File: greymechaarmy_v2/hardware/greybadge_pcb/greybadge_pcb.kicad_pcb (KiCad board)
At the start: 2 copper layers, 75 x 99 mm, 155 parts, among them J1 Conn_02x05_Row_Letter_First, J2 Conn_02x05_Row_Letter_First, J3 Conn_02x05_Row_Letter_First, J4 JST PH S2B, J5 USB_C_Receptacle_USB2.0, J6 Conn_02x05_Row_Letter_First, Q1 2N7002, Q2 Q_NMOS_GSD, SW1 SW_Push, SW10 SW_Push, SW2 SW_Push, SW3 SW_Push, SW4 SW_Push, SW5 SW_Push, SW6 SW_Push, SW7 SW_Push, SW8 SW_SPDT, SW9 SW_Push, U1 APS6404L-3SQR-SN_C5333729, U10 AMS1117-3.3, U2 TLV73311PDBV, U3 TLV73325PDBV, U4 GC9A01_IPS_display, U5 BQ24075, U6 W25Q128JVS, U7 RP2350_60QFN, U8 ECP5U_25_CABGA256, U9 W25Q128JVSIM, X1 SiT2001B, Y1 12Mhz

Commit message: feat: improve art
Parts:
- added G***: LOGO, LOGO, F.Cu at (96.2, 65.4)
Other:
- board text added: "C4[2] C6[6] D3[1] C5[4] D5[5] C3[0] D4[3] D6[7]"
- board text added: "LEDs"

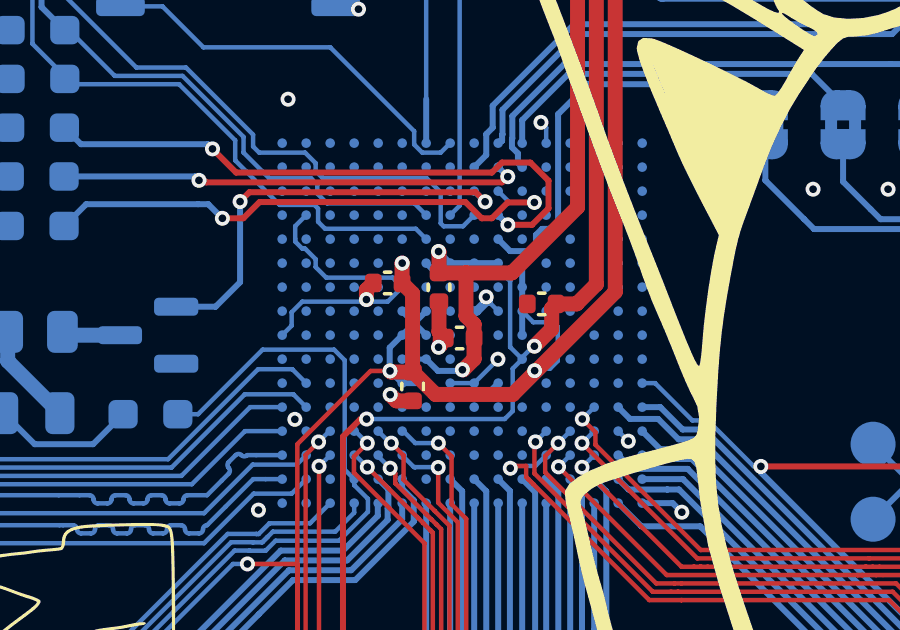
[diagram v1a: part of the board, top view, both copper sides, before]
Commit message: feat: change from via in pad to via out of pad
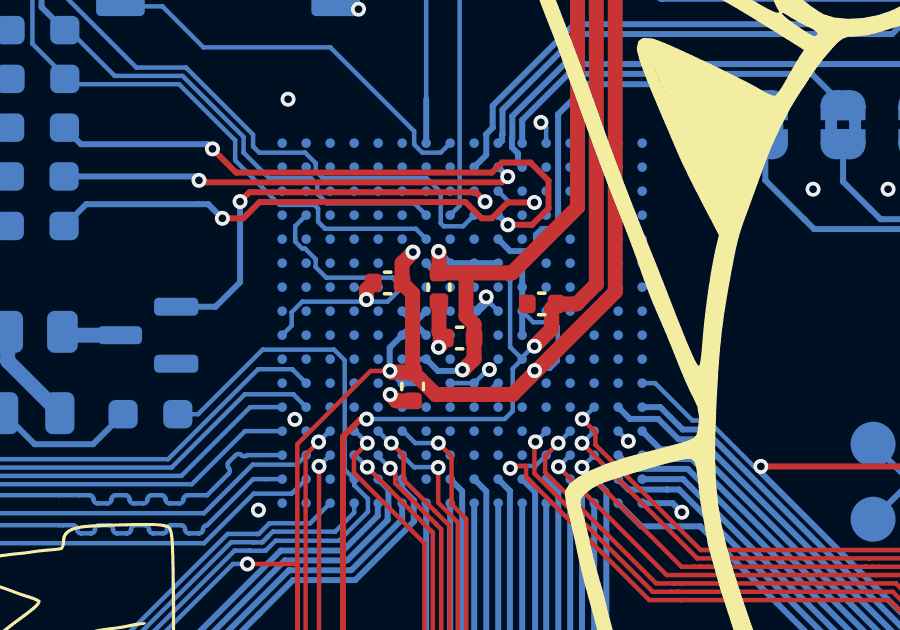
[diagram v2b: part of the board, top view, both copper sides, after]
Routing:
- net +3V3: track 351.5 -> 352.5 mm
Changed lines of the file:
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@@
 	)
 	(via
-		(at 105.494879 89.167232)
+		(at 105.210603 89.511917)
 		(size 0.5)
 		(drill 0.254)
@@
 	)
 	(segment
+		(start 105.210603 89.511917)
+		(end 105.155509 89.511917)
+		(width 0.15)
+		(layer "B.Cu")
+		(net 1)
+	)
+	(segment
 		(start 144.050825 102.618538)
 		(end 144.046666 102.614379)
@@
 	)
 	(segment
+		(start 105.155509 89.511917)
+		(end 104.703599 89.963827)
+		(width 0.15)
+		(layer "B.Cu")
+		(net 1)
+	)
+	(segment
 		(start 115.532342 70.675058)
 		(end 115.5446 70.6628)
@@
 	)
 	(segment
-		(start 105.503599 89.163827)
-		(end 104.703599 89.963827)
-		(width 0.15)
-		(layer "B.Cu")
-		(net 1)
-	)
-	(segment
 		(start 136.161298 105.209702)
 		(end 136.1694 105.2016)
@@
 		(end 122.5 78.5)
 		(width 0.2)
-		(layer "B.Cu")
-		(net 1)
-	)
-	(segment
-		(start 105.498284 89.163827)
-		(end 105.494879 89.167232)
-		(width 0.15)
 		(layer "B.Cu")
 		(net 1)
@@
 		(start 99.066491 85.479827)
 		(end 98.972707 85.479827)
-		(width 0.15)
-		(layer "B.Cu")
-		(net 1)
-	)
-	(segment
-		(start 105.503599 89.163827)
-		(end 105.498284 89.163827)
 		(width 0.15)
 		(layer "B.Cu")
@@
 	)
 	(segment
+		(start 102.3 85.967426)
+		(end 102.3 86.65)
+		(width 0.5)
+		(layer "F.Cu")
+		(net 2)
+	)
+	(segment
 		(start 102.65 86.975)
 		(end 102.3 86.625)
@@
 	)
 	(segment
+		(start 102.661626 85.596853)
+		(end 102.661626 85.6058)
+		(width 0.5)
+		(layer "F.Cu")
+		(net 2)
+	)
+	(segment
 		(start 102.669976 89.595)
 		(end 103.415863 90.340887)
@@
 	)
 	(segment
-		(start 102.3 86.65)
-		(end 102.3 85.967426)
-		(width 0.5)
-		(layer "F.Cu")
-		(net 2)
-	)
-	(segment
 		(start 98.807391 95.99075)
 		(end 98.807391 98.589551)
@@
 	)
 	(segment
-		(start 102.3 85.967426)
-		(end 102.303599 85.963827)
-		(width 0.5)
-		(layer "F.Cu")
-		(net 2)
-	)
-	(segment
 		(start 136.3218 103.505)
 		(end 136.367699 103.459101)
+		(width 0.5)
+		(layer "F.Cu")
+		(net 2)
+	)
+	(segment
+		(start 102.661626 85.6058)
+		(end 102.3 85.967426)
 		(width 0.5)
 		(layer "F.Cu")
@@
 	)
 	(via
-		(at 102.303599 85.963827)
+		(at 102.661626 85.596853)
 		(size 0.5)
 		(drill 0.254)
@@
 	)
 	(segment
+		(start 102.303599 85.963827)
+		(end 102.303599 85.95488)
+		(width 0.15)
+		(layer "B.Cu")
+		(net 2)
+	)
+	(segment
 		(start 106.303599 87.563827)
 		(end 106.303599 88.363827)
@@
 		(layer "B.Cu")
 		(net 2)
+	)
+	(segment
+		(start 102.303599 85.95488)
+		(end 102.661626 85.596853)
+		(width 0.15)
+		(layer "B.Cu")
+		(net 2)
